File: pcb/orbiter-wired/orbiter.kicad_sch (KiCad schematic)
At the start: 19 parts, among them J1 SWD, J3 I2C Extension, J5 Keyboard matrix, U1 TPS82140SILR, U2 USBLC6-2P6

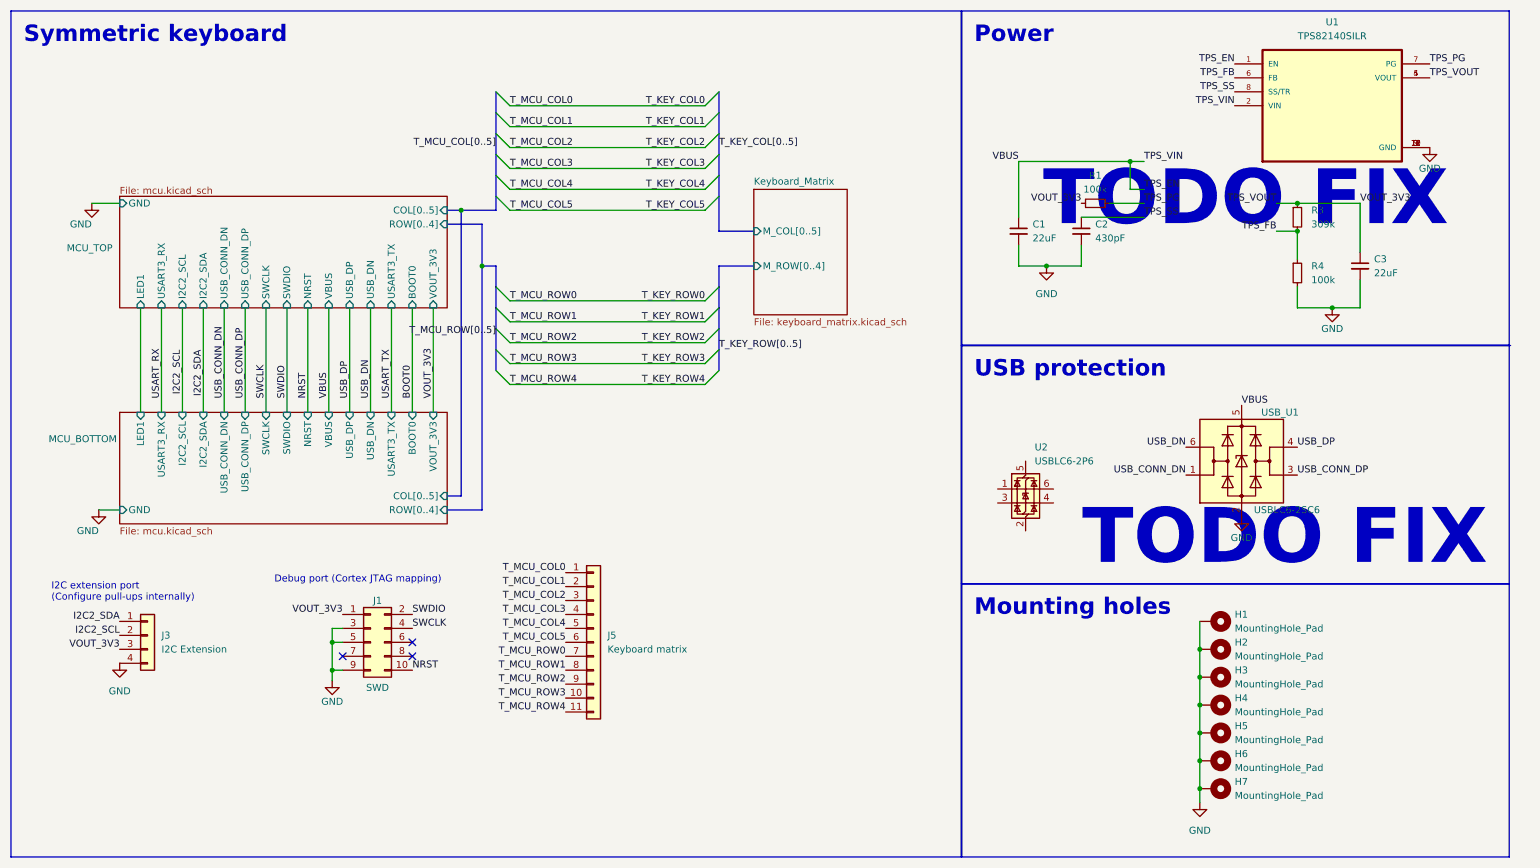
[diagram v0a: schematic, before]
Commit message: Bump to Kicad 9
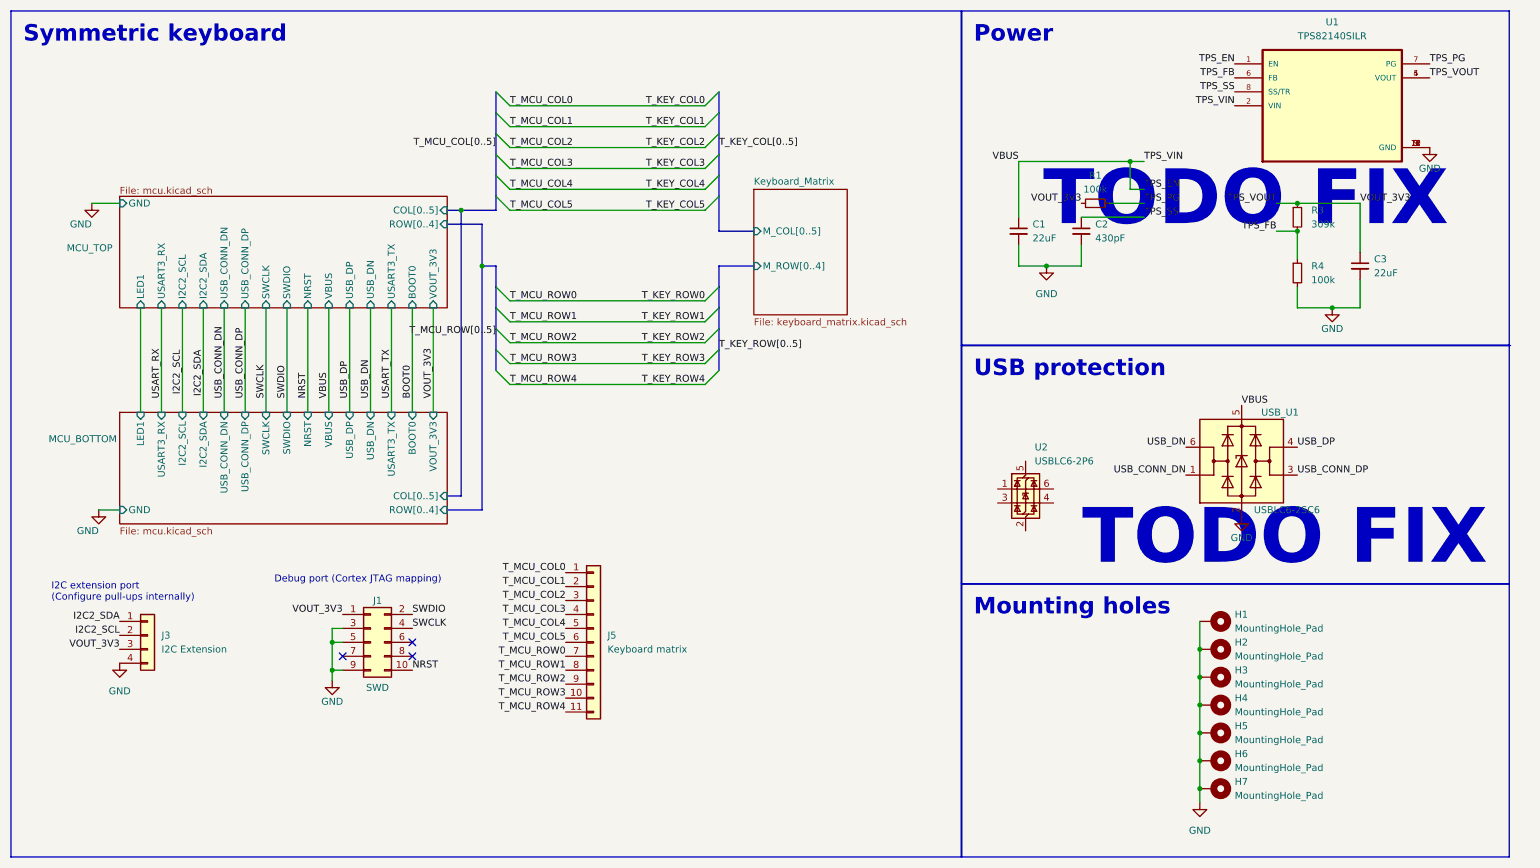
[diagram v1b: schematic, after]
